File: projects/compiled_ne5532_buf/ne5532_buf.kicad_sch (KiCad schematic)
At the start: 3 parts, among them U1 NE5532

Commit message: F5: human-quality pass — weld, route beauty, silent flags, design guide
The user's mandate: schematics must read as hand-drawn — tidy wires over
tag pairs, clean corners, nothing on screen but symbol, model and value.

- internal/place2/weld: same-net label islands get welded into real wires
  (straight/L/Z) whenever a clean corridor exists; every candidate is
  validated against gate.Check and reverted on any new violation. Redundant
  labels removed, one kept as documentation.
- routeNets beauty policy: a path with more than 3 bends or >70% detour
  over Manhattan distance reads worse than a label — demoted before it is
  ever drawn. Combined with weld this replaces snakes with short wires.
- PWR_FLAG value text hidden (sexp.HidePropertyText): the flag exists for
  ERC, not for the reader.
- design_guide: human-schematic conventions (signal flow, wire-vs-label,
  spacing recipes in grid cells, iteration protocol) distilled from
  SparkFun/KLC/IEEE-315/Altium/H&H research, embedded in the binary and
  served as an MCP tool for authoring LLMs.
- Crystal clusters reworked in both MCU sources: vertical crystal, straight
  XTAL1, single-L XTAL2, horizontal load caps — full Pierce oscillator
  wiring, zero label pairs. NE555 timing chain now fully wired via weld.

Co-Authored-By: Claude Fable 5 <noreply@anthropic.com>
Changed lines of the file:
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@@
     (instances
       (project ""
-        (path "/61e331b2-6927-41fb-be59-2b45964ad494" (reference "U1") (unit 1)))))
+        (path "/f34e73de-a24a-4018-9fe9-425063a44897" (reference "U1") (unit 1)))))
   (symbol (lib_id "Amplifier_Operational:NE5532")
     (at 33.02 48.26 0) (unit 2) (exclude_from_sim no) (in_bom yes) (on_board yes) (dnp no)
@@
     (instances
       (project ""
-        (path "/61e331b2-6927-41fb-be59-2b45964ad494" (reference "U1") (unit 2)))))
+        (path "/f34e73de-a24a-4018-9fe9-425063a44897" (reference "U1") (unit 2)))))
   (symbol (lib_id "Amplifier_Operational:NE5532")
     (at 68.58 35.56 0) (unit 3) (exclude_from_sim no) (in_bom yes) (on_board yes) (dnp no)
@@
     (instances
       (project ""
-        (path "/61e331b2-6927-41fb-be59-2b45964ad494" (reference "U1") (unit 3)))))
+        (path "/f34e73de-a24a-4018-9fe9-425063a44897" (reference "U1") (unit 3)))))
   (symbol (lib_id "Device:C")
     (at 81.28 31.75 0) (unit 1) (exclude_from_sim no) (in_bom yes) (on_board yes) (dnp no)
@@
     (instances
       (project ""
-        (path "/61e331b2-6927-41fb-be59-2b45964ad494" (reference "C1") (unit 1)))))
+        (path "/f34e73de-a24a-4018-9fe9-425063a44897" (reference "C1") (unit 1)))))
   (symbol (lib_id "Device:C")
     (at 81.28 39.37 0) (unit 1) (exclude_from_sim no) (in_bom yes) (on_board yes) (dnp no)
@@
     (instances
       (project ""
-        (path "/61e331b2-6927-41fb-be59-2b45964ad494" (reference "C2") (unit 1)))))
+        (path "/f34e73de-a24a-4018-9fe9-425063a44897" (reference "C2") (unit 1)))))
   (symbol (lib_id "power:GND")
     (at 22.86 25.4 270) (unit 1) (exclude_from_sim no) (in_bom no) (on_board no) (dnp no)
@@
     (instances
       (project ""
-        (path "/61e331b2-6927-41fb-be59-2b45964ad494" (reference "#PWR01") (unit 1)))))
+        (path "/f34e73de-a24a-4018-9fe9-425063a44897" (reference "#PWR01") (unit 1)))))
   (wire
     (pts (xy 25.4 25.4) (xy 22.86 25.4))
@@
     (instances
       (project ""
-        (path "/61e331b2-6927-41fb-be59-2b45964ad494" (reference "#PWR02") (unit 1)))))
+        (path "/f34e73de-a24a-4018-9fe9-425063a44897" (reference "#PWR02") (unit 1)))))
   (wire
     (pts (xy 25.4 45.72) (xy 22.86 45.72))
@@
     (instances
       (project ""
-        (path "/61e331b2-6927-41fb-be59-2b45964ad494" (reference "#PWR03") (unit 1)))))
+        (path "/f34e73de-a24a-4018-9fe9-425063a44897" (reference "#PWR03") (unit 1)))))
   (wire
     (pts (xy 81.28 35.56) (xy 81.28 38.1))
@@
     (instances
       (project ""
-        (path "/61e331b2-6927-41fb-be59-2b45964ad494" (reference "#PWR04") (unit 1)))))
+        (path "/f34e73de-a24a-4018-9fe9-425063a44897" (reference "#PWR04") (unit 1)))))
   (wire
     (pts (xy 81.28 35.56) (xy 81.28 33.02))
@@
     (instances
       (project ""
-        (path "/61e331b2-6927-41fb-be59-2b45964ad494" (reference "#PWR05") (unit 1)))))
+        (path "/f34e73de-a24a-4018-9fe9-425063a44897" (reference "#PWR05") (unit 1)))))
   (wire
     (pts (xy 66.04 43.18) (xy 66.04 45.72))
@@
     (instances
       (project ""
-        (path "/61e331b2-6927-41fb-be59-2b45964ad494" (reference "#PWR06") (unit 1)))))
+        (path "/f34e73de-a24a-4018-9fe9-425063a44897" (reference "#PWR06") (unit 1)))))
   (wire
     (pts (xy 81.28 43.18) (xy 81.28 45.72))
@@
     (instances
       (project ""
-        (path "/61e331b2-6927-41fb-be59-2b45964ad494" (reference "#PWR07") (unit 1)))))
+        (path "/f34e73de-a24a-4018-9fe9-425063a44897" (reference "#PWR07") (unit 1)))))
   (wire
     (pts (xy 66.04 27.94) (xy 66.04 25.4))
@@
     (instances
       (project ""
-        (path "/61e331b2-6927-41fb-be59-2b45964ad494" (reference "#PWR08") (unit 1)))))
+        (path "/f34e73de-a24a-4018-9fe9-425063a44897" (reference "#PWR08") (unit 1)))))
   (wire
     (pts (xy 81.28 27.94) (xy 81.28 25.4))
@@
         (font (size 1.27 1.27)) (hide yes)))
     (property "Value" "PWR_FLAG"
-      (at 87.75 27.94 0)
-      (effects
-        (font (size 1.27 1.27))))
+      (at 78.74 25.4 0)
+      (effects
+        (font (size 1.27 1.27)) (hide yes)))
     (property "Footprint" ""
       (at 78.74 27.94 0)
@@
     (instances
       (project ""
-        (path "/61e331b2-6927-41fb-be59-2b45964ad494" (reference "#FLG01") (unit 1)))))
+        (path "/f34e73de-a24a-4018-9fe9-425063a44897" (reference "#FLG01") (unit 1)))))
   (wire
     (pts (xy 81.28 27.94) (xy 78.74 27.94))
@@
         (font (size 1.27 1.27)) (hide yes)))
     (property "Value" "PWR_FLAG"
-      (at 87.75 43.18 0)
-      (effects
-        (font (size 1.27 1.27))))
+      (at 78.74 45.72 0)
+      (effects
+        (font (size 1.27 1.27)) (hide yes)))
     (property "Footprint" ""
       (at 78.74 43.18 0)
@@
     (instances
       (project ""
-        (path "/61e331b2-6927-41fb-be59-2b45964ad494" (reference "#FLG02") (unit 1)))))
+        (path "/f34e73de-a24a-4018-9fe9-425063a44897" (reference "#FLG02") (unit 1)))))
   (wire
     (pts (xy 81.28 43.18) (xy 78.74 43.18))
@@
         (font (size 1.27 1.27)) (hide yes)))
     (property "Value" "PWR_FLAG"
-      (at 87.75 35.56 0)
-      (effects
-        (font (size 1.27 1.27))))
+      (at 78.74 38.1 0)
+      (effects
+        (font (size 1.27 1.27)) (hide yes)))
     (property "Footprint" ""
       (at 78.74 35.56 0)
@@
     (instances
       (project ""
-        (path "/61e331b2-6927-41fb-be59-2b45964ad494" (reference "#FLG03") (unit 1)))))
+        (path "/f34e73de-a24a-4018-9fe9-425063a44897" (reference "#FLG03") (unit 1)))))
   (wire
     (pts (xy 81.28 35.56) (xy 78.74 35.56))

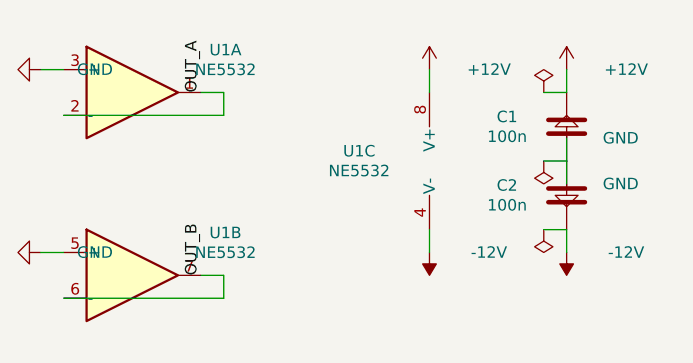
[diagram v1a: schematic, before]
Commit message: Body model sees real symbol graphics; quiet nets drop junction tags
User-reported flaws from visual review, both fixed at the root:

- Wires over symbol artwork: the body model was pin-derived and blind to
  drawn graphics — an op-amp triangle's vertices stick out beyond the pin
  box, so "legal" wires crossed the drawing. internal/sexp/graphics.go now
  parses rectangle/polyline/circle/arc/bezier extents per unit with the
  exact pin transform; metrics.BodyBBox unions them with the legacy box,
  clamped off pin tips (Device:LED's emission arrows overhang the cathode
  pin and would have swallowed it). NE5532 feedback: 8 stroke crossings
  through the triangle before, 0 after (loops now label pairs). The model
  also exposed genuinely bad baked geometry in mcu_minimal_atmega328's
  crystal — repositioned with the template contract intact.

- "ANODE" tag on a resistor leg: net names with a "_" prefix are now
  quiet — connectivity only, their documentation label is stripped at the
  end of compilation when the wiring alone keeps the net whole. Junction
  nodes (R->LED) stay unlabeled like in any hand-drawn schematic.

- Battery hump: led_18650 anchors R1 in the pin's exit direction; the
  design guide gains the "respect the pin's exit direction" and "internal
  junctions carry no tag" recipes.

Co-Authored-By: Claude Fable 5 <noreply@anthropic.com>
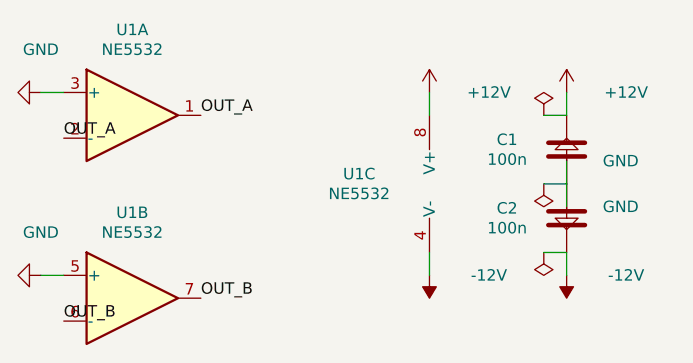
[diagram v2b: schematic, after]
